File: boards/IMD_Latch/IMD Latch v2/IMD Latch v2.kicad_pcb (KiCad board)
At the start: 2 copper layers, 0 parts

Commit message: IMD Latch V2 Layout
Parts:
- added C1: C_10uF, footprints:C_0805_OEM, F.Cu at (151.4, 103.8)
- added D1: D_Zener_18V, footprints:DO-214AA, F.Cu at (153.4, 93.9)
- added D2: LED_0805, footprints:LED_0805_OEM, F.Cu at (155.8, 98.2)
- added D3: LED_0805, footprints:LED_0805_OEM, F.Cu at (149.4, 112.8)
- added D4: D_Schottky_SOD123, footprints:D_SOD-123W_OEM, F.Cu at (158.6, 112.3)
- added F1: 500mA, footprints:Fuse_1210, F.Cu at (151.3, 97.8)
- added J1: micromatch_female_RA_8, footprints:micromatch_female_ra_8, F.Cu at (141.9, 108.2)
- added J2: Ultrafit_2, footprints:Ultrafit_2, F.Cu at (167.8, 96.4)
- added K1: G5Q-1A4-DC5-5V, footprints:Relay_SPST_OMRON-G5Q-1A4_OEM, F.Cu at (157.7, 109.0)
- added Q1: SSM3K333R, footprints:SOT-23F, F.Cu at (159.9, 98.0)
- added R1: R_1k, footprints:R_0805_OEM, F.Cu at (158.5, 93.9)
- added R2: R_604k, footprints:R_0805_OEM, F.Cu at (148.3, 103.9)
- added R3: R_1.82M, footprints:R_0805_OEM, F.Cu at (154.7, 103.8)
- added R4: R_1M, footprints:R_0805_OEM, F.Cu at (152.9, 100.7)
- added R5: R_1k, footprints:R_0805_OEM, F.Cu at (154.1, 112.8)
- added R6: R_2.2k, footprints:R_0805_OEM, F.Cu at (149.0, 100.6)
- added U1: CD4043BPWR, footprints:TSSOP-16-OEM, F.Cu at (151.2, 108.6)
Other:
- board outline added: 40 x 35 mm

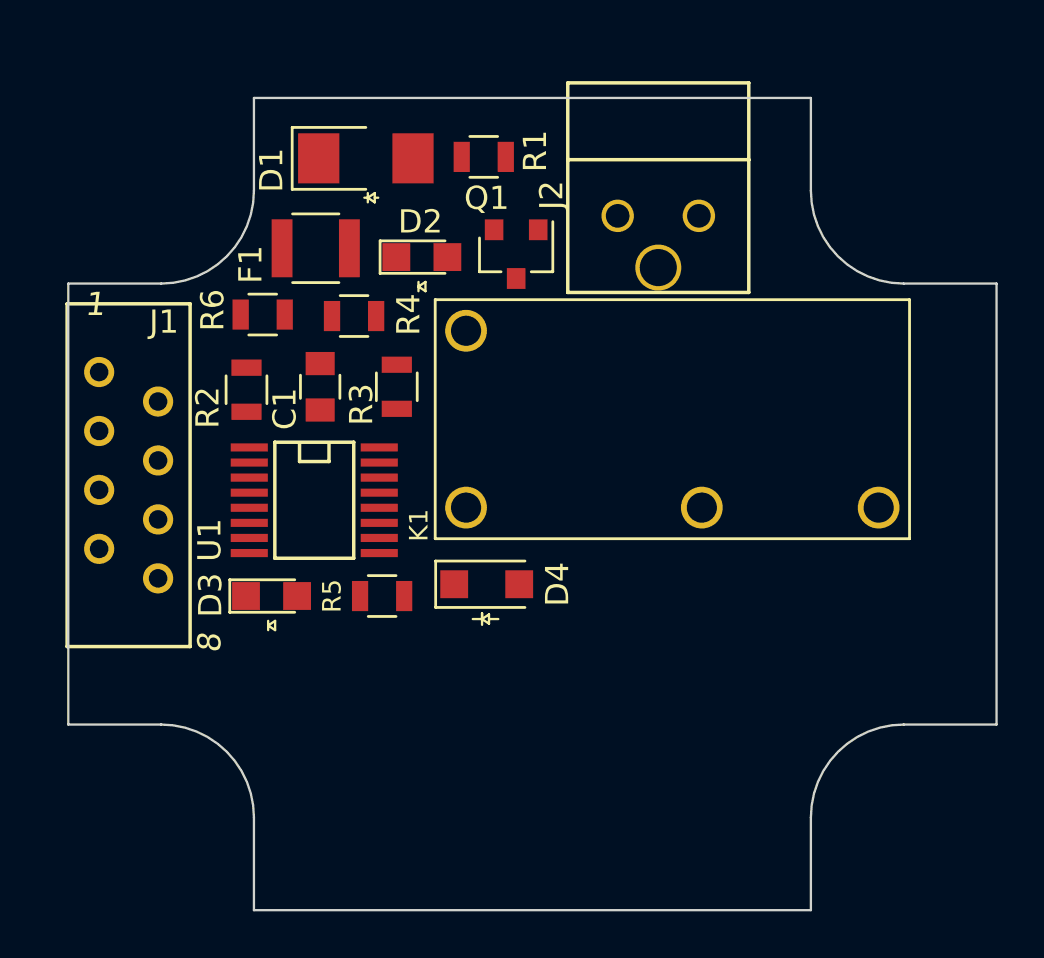
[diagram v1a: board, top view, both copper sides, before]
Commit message: IMD Latch v2 finished Layout/Routing
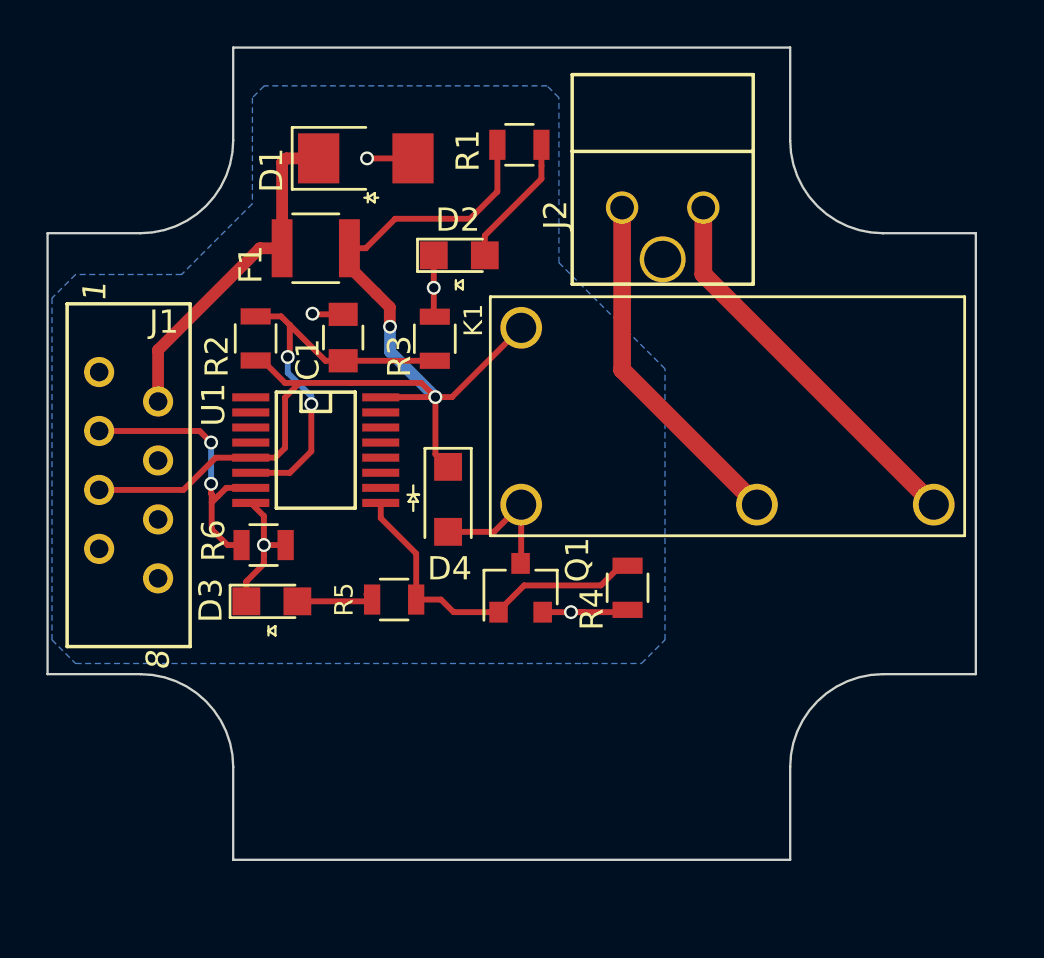
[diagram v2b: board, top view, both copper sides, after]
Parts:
- R2: value R_604k -> R_576k
- R3: value R_1.82M -> R_2.94M
- moved R4 16.6 mm to (164.7, 112.4), turned to 270 degrees
- moved Q1 14.4 mm to (160.1, 112.4), turned to 90 degrees
- moved R6 9.93 mm to (149.0, 110.6)
- moved D4 4.02 mm to (157.0, 108.6), turned to 270 degrees
- moved R3 2.64 mm to (156.4, 101.7)
- moved K1 2.38 mm to (160.1, 108.8)
- moved C1 2.34 mm to (152.4, 101.6)
- moved R2 2.24 mm to (148.7, 101.7)
- moved U1 2.16 mm to (151.3, 106.5)
- moved R1 1.62 mm to (160.0, 93.3), turned to 0 degrees
- moved D2 1.61 mm to (157.4, 98.1)
- moved R5 0.54 mm to (154.6, 112.9)
- moved J2 0.40 mm to (168.0, 96.0)
- moved D3 0.23 mm to (149.4, 113.0)
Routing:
- net /12V_Fused: track 0.00 -> 48.1 mm, vias 0 -> 2
- net Net-(C1-Pad1): track 0.00 -> 17.4 mm, vias 0 -> 2
- net Net-(J2-Pad2): track 0.00 -> 16.9 mm
- net GND: track 0.00 -> 15.9 mm, vias 0 -> 5
- net Net-(J2-Pad1): track 0.00 -> 15.2 mm
- net Net-(Q1-Pad1): track 0.00 -> 15.0 mm
- net +12V: track 0.00 -> 14.7 mm
- net Net-(J1-Pad3): track 0.00 -> 12.3 mm, vias 0 -> 2
- net Net-(D4-Pad2): track 0.00 -> 6.18 mm
- net Net-(D2-Pad2): track 0.00 -> 5.77 mm
- net Net-(D3-Pad2): track 0.00 -> 3.27 mm
- added copper zone on B.Cu, net GND

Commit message: IMD Latch v2 not yet checked off
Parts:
- moved D4 12.9 mm to (169.4, 112.1), turned to 180 degrees
- moved K1 2.09 mm to (158.1, 109.2)
- moved R3 0.88 mm to (155.5, 101.7)
- moved J2 0.65 mm to (167.4, 95.7)
- moved R1 0.20 mm to (159.8, 93.3)
- moved U1 0.19 mm to (151.1, 106.5)
- moved C1 0.05 mm to (152.4, 101.6)
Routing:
- net /12V_Fused: track 48.1 -> 59.8 mm
- net Net-(D4-Pad2): track 6.18 -> 11.9 mm
- net GND: track 15.9 -> 19.5 mm, vias 5 -> 4
- net Net-(C1-Pad1): track 17.4 -> 16.1 mm
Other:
- board size 40 x 35 mm -> 37 x 32 mm
- board text added: "12V LED"
- board text added: "IMD Latch V2"
- board text added: "Josh Deng"
- board text added: "NOR Latch LED"
- board text added: "Olin Electric Motorsports"

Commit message: Finished & Shipped IMD Latch v2
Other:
- outline, holes or cut-outs redrawn
- net class Default: via_dia 0.6 -> 0.6096; via_drill 0.4 -> 0.3048
- rule via_min_drill: 0.3 -> 0.3048
- rule via_min_size: 0.4 -> 0.6096
